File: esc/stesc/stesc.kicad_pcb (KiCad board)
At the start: 4 copper layers, 78.4 x 29.7 mm, 37 parts, among them J1 USB_C_Receptacle_USB2.0, J2 Conn_01x04, J3 5530843-7, SW1 SW_Push, SW2 SW_Push, U1 RP2040, U2 W25Q64JVXGIQ, U3 B-G431B-ESC1, Y1 12MHz

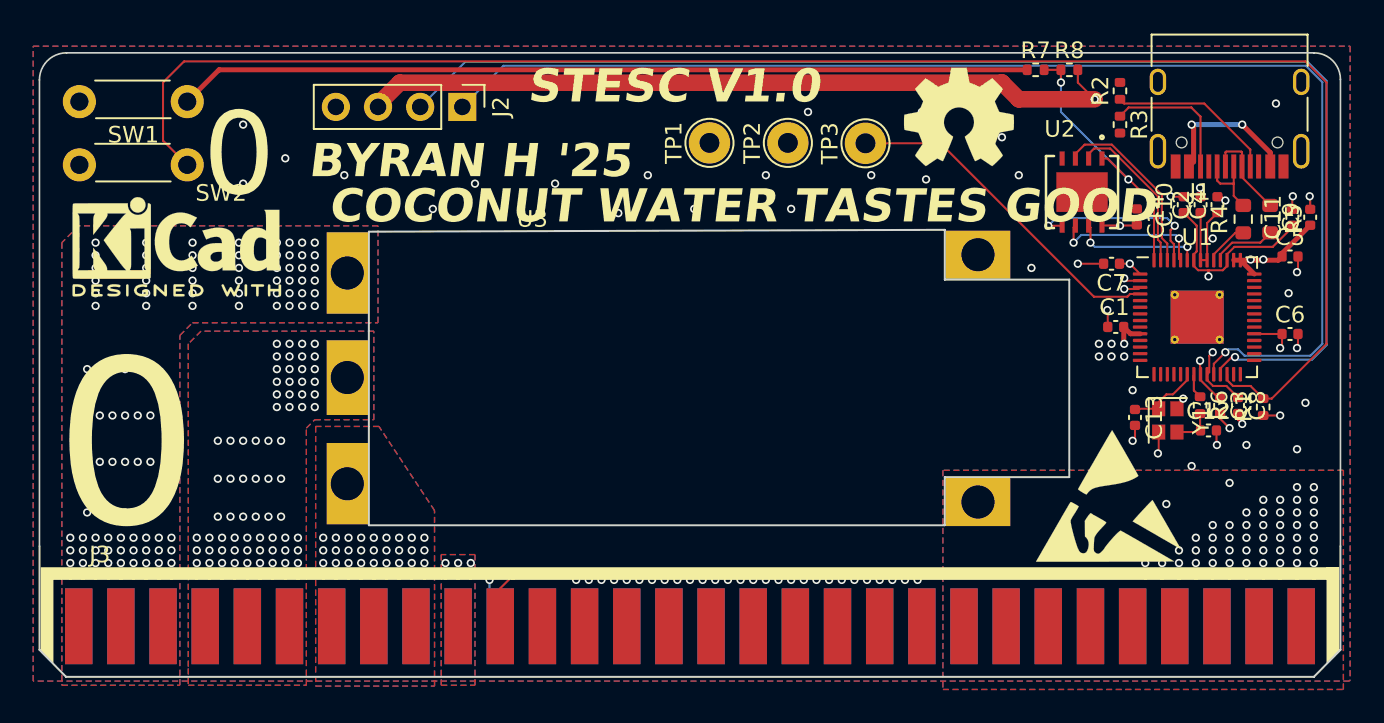
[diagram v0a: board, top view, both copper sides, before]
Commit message: Feat[stesc]: v1.0 draft complete
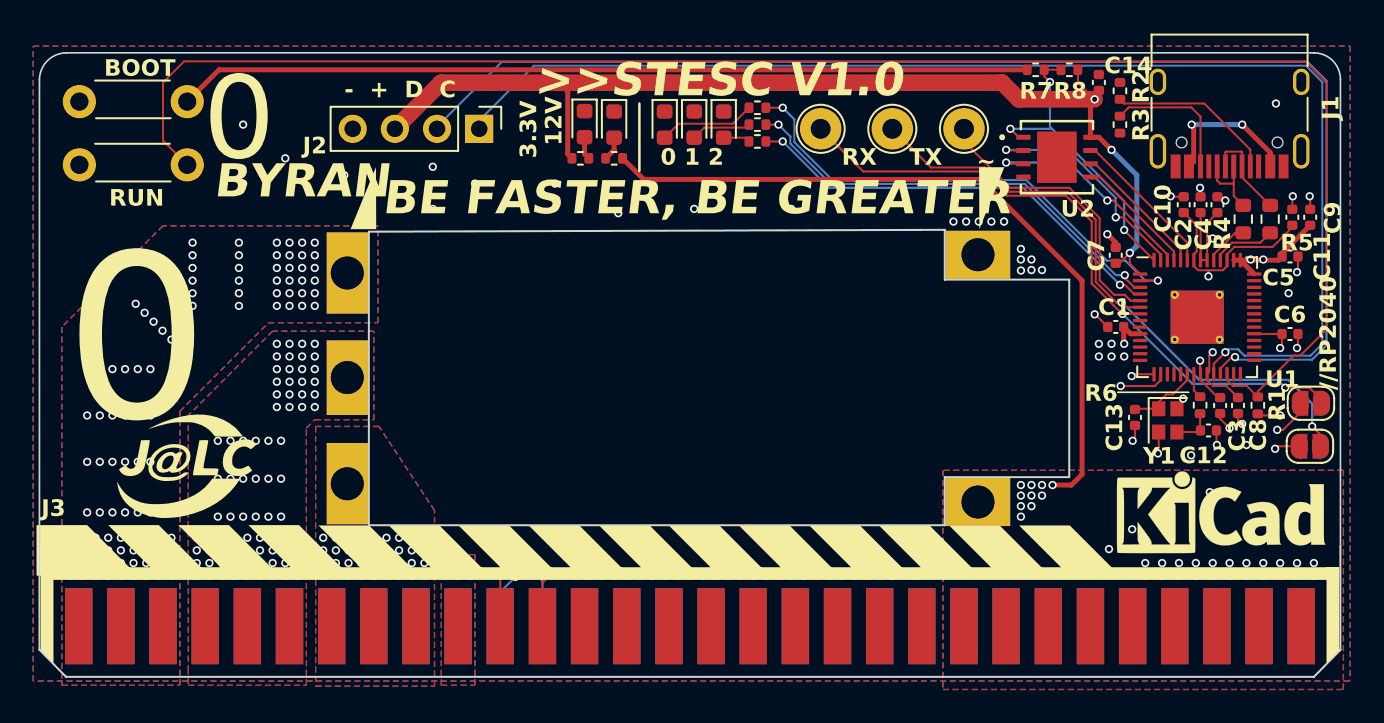
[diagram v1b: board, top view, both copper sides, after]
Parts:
- removed the REF** at (139.0, 104.1)
- removed the REF** at (195.2, 119.1)
- added D1: LED, LED_SMD:LED_0603_1608Metric, F.Cu at (163.6, 96.7)
- added D2: LED, LED_SMD:LED_0603_1608Metric, F.Cu at (165.4, 96.8)
- added D3: LED0, LED_SMD:LED_0603_1608Metric, F.Cu at (168.4, 96.8)
- added D4: LED1, LED_SMD:LED_0603_1608Metric, F.Cu at (170.2, 96.8)
- added D5: LED2, LED_SMD:LED_0603_1608Metric, F.Cu at (172.0, 96.8)
- added G***: LOGO, JLCPCB_Logo:JLCPCB_Logo_Black, F.Cu at (139.7, 117.3)
- added G***: LOGO, JLCPCB_Logo:JLCPCB_Logo_Black, B.Cu at (139.6, 117.4)
- added JP2: RX, Jumper:SolderJumper-2_P1.3mm_Open_RoundedPad1.0x1.5mm, F.Cu at (207.3, 113.6)
- added JP3: TX, Jumper:SolderJumper-2_P1.3mm_Open_RoundedPad1.0x1.5mm, F.Cu at (207.3, 116.2)
- added R10: 1k, Resistor_SMD:R_0402_1005Metric, F.Cu at (165.4, 98.8)
- added R11: 1k, Resistor_SMD:R_0402_1005Metric, F.Cu at (174.0, 95.8)
- added R12: 1k, Resistor_SMD:R_0402_1005Metric, F.Cu at (174.0, 96.8)
- added R13: 1k, Resistor_SMD:R_0402_1005Metric, F.Cu at (174.0, 97.8)
- added R9: 1k, Resistor_SMD:R_0402_1005Metric, F.Cu at (163.3, 98.8)
- added REF**: KiCad-Logo_5mm_SilkScreen, Symbol:KiCad-Logo_5mm_SilkScreen, F.Cu at (201.9, 120.7)
- added REF**: ESD-Logo_6.6x6mm_SilkScreen, Symbol:ESD-Logo_6.6x6mm_SilkScreen, B.Cu at (205.5, 119.9)
- REF**: moved to B.Cu
- moved REF** 26.3 mm to (197.9, 119.9), turned to 180 degrees
- moved TP1 11.0 mm to (182.1, 97.0)
- moved C14 8.42 mm to (194.6, 94.2)
- moved TP3 6.00 mm to (186.4, 97.0)
- moved U2 2.59 mm to (192.0, 98.7), turned to 0 degrees
- moved TP2 2.15 mm to (177.8, 97.0)
- moved J2 1.67 mm to (157.2, 97.0)
- moved C7 0.57 mm to (195.6, 104.6), turned to 90 degrees
- moved R1 0.34 mm to (204.1, 113.7)
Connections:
- TP1 pad 1: unconnected-(TP1-Pad1) -> /UART1_TX
- TP2 pad 1: unconnected-(TP2-Pad1) -> /UART1_RX
- U1 pad 15: unconnected-(U1-GPIO12-Pad15) -> /BOARD_TX
- U1 pad 16: unconnected-(U1-GPIO13-Pad16) -> /BOARD_RX
- U1 pad 2: /BOARD_TX -> /RP2040/LED0
- U1 pad 3: /BOARD_RX -> /RP2040/LED1
- U1 pad 4: /ESC_PWM -> /RP2040/LED2
- U1 pad 5: /RP2040/NEOPIXEL -> /ESC_PWM
- U1 pad 6: unconnected-(U1-GPIO4-Pad6) -> /UART1_TX
- U1 pad 7: unconnected-(U1-GPIO5-Pad7) -> /UART1_RX
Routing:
- net /BOARD_RX_1: track 0.00 -> 54.4 mm, vias 0 -> 2
- net /BOARD_TX_1: track 0.00 -> 52.5 mm, vias 0 -> 2
- net +12V: track 0.00 -> 44.5 mm, vias 60 -> 32
- net /UART1_RX: track 0.00 -> 40.4 mm, vias 0 -> 2
- net /UART1_TX: track 0.00 -> 38.5 mm, vias 0 -> 2
- net /RP2040/LED0: track 0.00 -> 29.8 mm, vias 0 -> 2
- net /RP2040/LED1: track 0.00 -> 27.0 mm, vias 0 -> 2
- net /RP2040/LED2: track 0.00 -> 26.4 mm, vias 0 -> 2
- net +3V3: track 129.1 -> 135.9 mm
- net /BOARD_TX: track 56.0 -> 49.9 mm
- net Net-(D3-A): track 0.00 -> 5.83 mm
- net /RP2040/QSPI_SD1: track 9.69 -> 14.0 mm, vias 0 -> 2
- net /RP2040/QSPI_SD0: track 11.1 -> 7.41 mm, vias 2 -> 0
- net Net-(D4-A): track 0.00 -> 3.63 mm
- net /BOARD_RX: track 54.5 -> 51.0 mm
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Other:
- board text added: "- + D C"
- board text added: "//RP2040"
- board text added: "0 1 2"
- board text added: "12V"
- board text added: "3.3V"
- board text added: ">>STESC ${REVISION}"
- board text added: "BE FASTER, BE GREATER"
- board text added: "BOOT"
- board text added: "BYRAN"
- board text added: "RP2040 8MB Flash USB-C UART0 + UART1 2 PWR LED 3 USER LED"
- board text added: "RUN"
- board text added: "RX"
- board text added: "TX"
- board text added: "~"
- board text removed: "BYRAN H '25"
- board text removed: "COCONUT WATER TASTES GOOD"
- board text removed: "STESC ${REVISION}"
